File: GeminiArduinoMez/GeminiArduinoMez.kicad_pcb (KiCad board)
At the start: 2 copper layers, 99.1 x 81.3 mm, 21 parts, among them J1 Conn_01x10, J2 CONN_06SILK_FEMALE_PTH, J3 CONN_06SILK_FEMALE_PTH, J4 Conn_02x10_Odd_Even, J5 POWER, J6 Switch, M1 Left MOTOR, M2 Right MOTOR, U1 DFRobot_DC_Controller

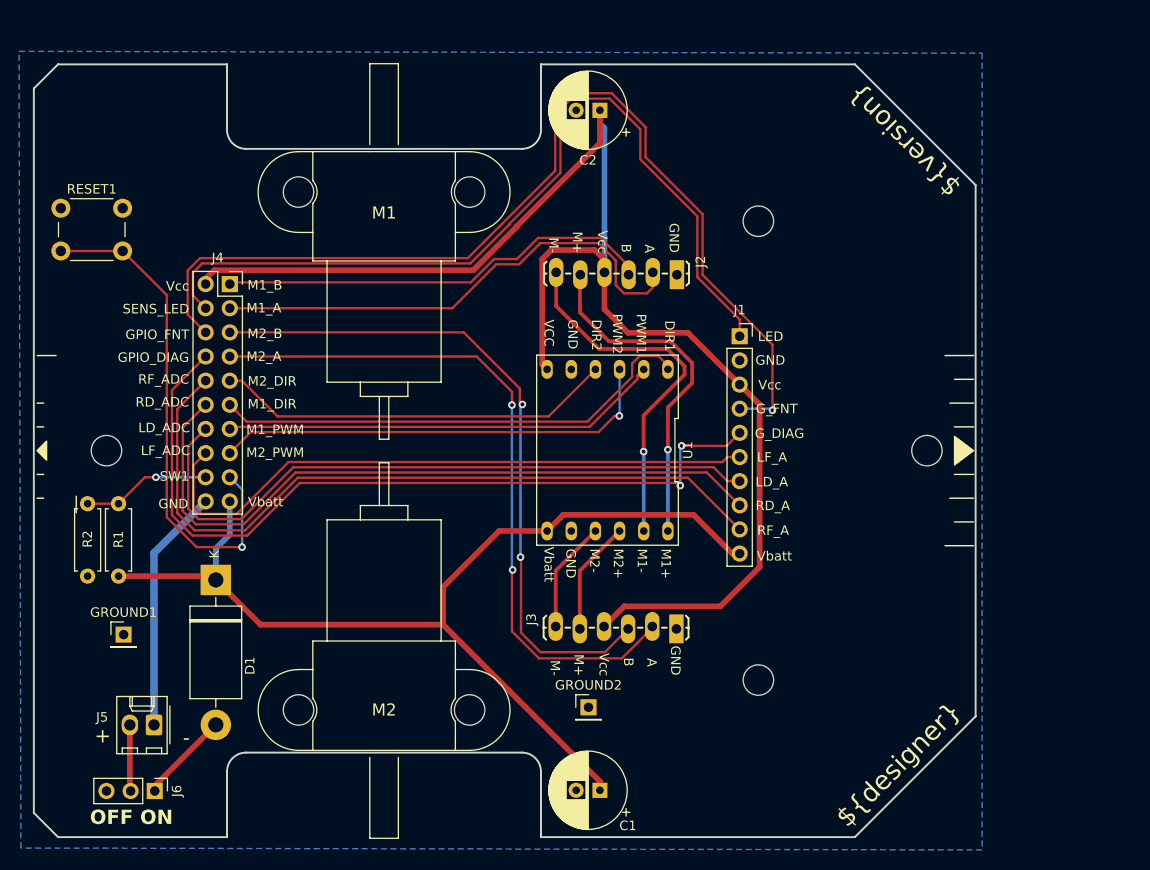
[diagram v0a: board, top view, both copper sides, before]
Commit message: Version 2 of boards sent to JLCPCB and a new calibration board
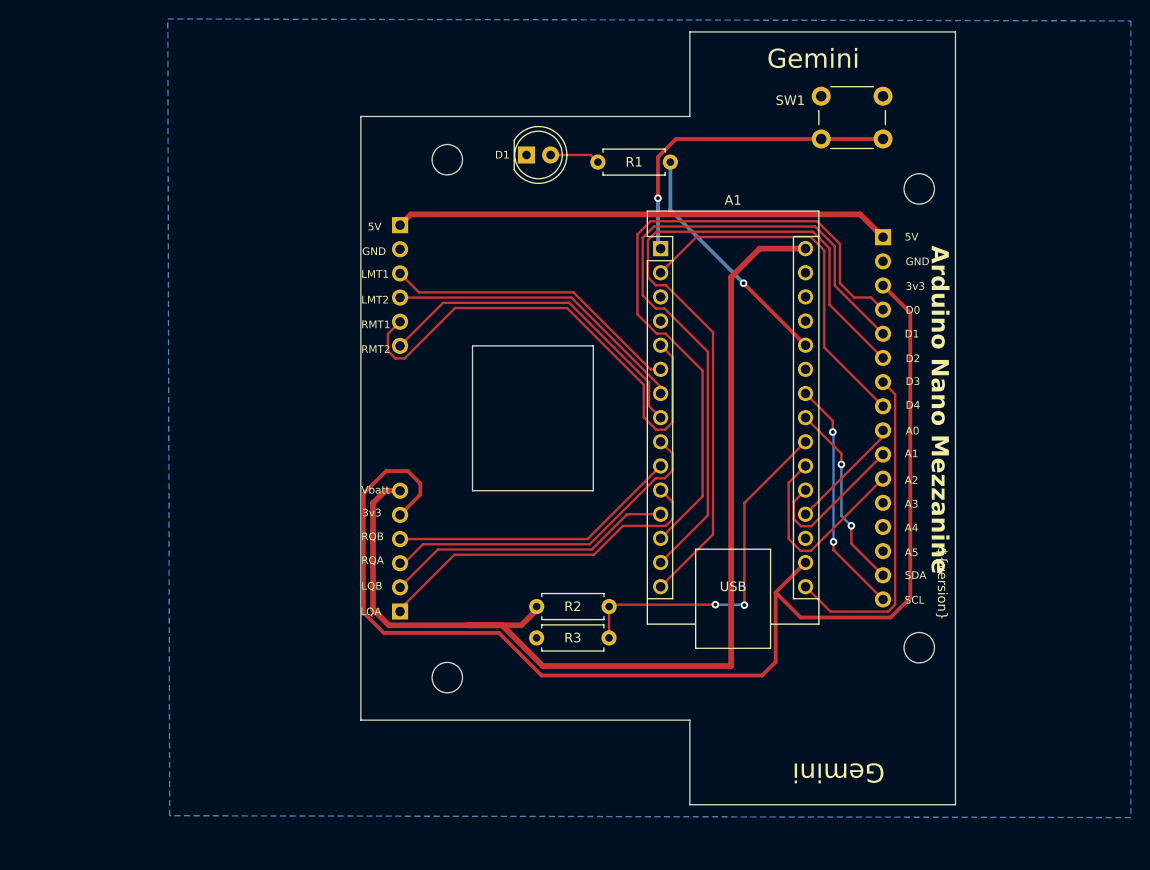
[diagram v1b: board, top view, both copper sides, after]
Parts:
- removed C1, C2: 330uF, 16V, Capacitor_THT:CP_Radial_D8.0mm_P2.50mm
- removed GROUND1, GROUND2: GROUND, Connector_PinHeader_2.54mm:PinHeader_1x01_P2.54mm_Vertical
- removed J2: CONN_06SILK_FEMALE_PTH, ukmarsbot:1X06_LOCK_LONGPADS
- removed J5: POWER, Connector_Molex:Molex_KK-254_AE-6410-02A_1x02_P2.54mm_Vertical
- removed J6: Switch, Connector_PinHeader_2.54mm:PinHeader_1x03_P2.54mm_Vertical
- removed M1: Left MOTOR, ukmarsbot:MINI-METAL-GEARMOTOR-WITH-BRACKET_Alt
- removed M2: Right MOTOR, ukmarsbot:MINI-METAL-GEARMOTOR-WITH-BRACKET
- removed RESET1: TACT_SW, Button_Switch_THT:SW_PUSH_6mm
- removed U1: DFRobot_DC_Controller, PBFootPrintLibrary:DFRobot_DC_Controller
- added A1: Arduino_Nano_RP2040_Connect, Module:Arduino_Nano, F.Cu at (134.1, 83.8)
- added R3: 68K, Resistor_THT:R_Axial_DIN0207_L6.3mm_D2.5mm_P7.62mm_Horizontal, F.Cu at (128.7, 124.7)
- added SW1: TACT_SW, Button_Switch_THT:SW_PUSH_6mm, F.Cu at (151.0, 67.7)
- D1: value 1N5401 -> LED; footprint Diode_THT:D_DO-201AD_P15.24mm_Horizontal -> LED_THT:LED_D5.0mm
- J1: value Conn_01x10 -> Conn_01x16; footprint Connector_PinSocket_2.54mm:PinSocket_1x10_P2.54mm_Vertical -> Connector_PinHeader_2.54mm:PinHeader_1x16_P2.54mm_Vertical; moved to B.Cu
- J3: value CONN_06SILK_FEMALE_PTH -> Conn_01x06; footprint ukmarsbot:1X06_LOCK_LONGPADS -> Connector_PinHeader_2.54mm:PinHeader_1x06_P2.54mm_Vertical; moved to B.Cu
- J4: value Conn_02x10_Odd_Even -> Conn_01x06; footprint Connector_PinSocket_2.54mm:PinSocket_2x10_P2.54mm_Vertical -> Connector_PinHeader_2.54mm:PinHeader_1x06_P2.54mm_Vertical; moved to B.Cu
- R1: value 180K -> 680R
- R2: value 68K -> 180K
- moved R1 72.6 mm to (135.1, 74.7), turned to 180 degrees
- moved H2 55.8 mm to (111.7, 128.9)
- moved D1 55.4 mm to (120.0, 73.9), turned to 0 degrees
- moved J3 51.5 mm to (106.7, 81.3), turned to 180 degrees
- moved R2 48.5 mm to (121.0, 121.4), turned to 0 degrees
- moved H1 47.1 mm to (111.7, 74.4)
- moved J4 38.8 mm to (106.7, 121.9)
- moved J1 18.3 mm to (157.5, 82.5), turned to 180 degrees
- moved H3 17.3 mm to (161.3, 77.5)
- moved H4 17.3 mm to (161.3, 125.7)
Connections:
- D1 pad 1: Vbatt -> GND
- D1 pad 2: /PWR -> Net-(D1-A)
- J1 pad 1: SENSOR_LED -> 5V
- J1 pad 10: Vbatt -> SEN1AIP
- J1 pad 3: Vcc -> 3v3
- J1 pad 4: GPIO_FRONT -> SEN0DI0
- J1 pad 5: GPIO_DIAG -> SEN1DI0
- J1 pad 6: LEFT_FRONT_ADC -> SEN2DI0
- J1 pad 7: LEFT_DIAG_ADC -> SEN3DI0
- J1 pad 8: RIGHT_DIAG_ADC -> SEN4DI0
- J1 pad 9: RIGHT_FRONT_ADC -> SEN0AIP
- J3 pad 1: GND -> 5V
- J3 pad 2: RIGHT_ENC_A -> GND
- J3 pad 3: RIGHT_ENC_B -> LMTR1
- J3 pad 4: Vcc -> LMTR2
- J3 pad 5: RIGHT_MOTOR_1 -> RMTR1
- J3 pad 6: RIGHT_MOTOR_2 -> RMTR2
- J4 pad 1: LEFT_ENC_B -> LQA
- J4 pad 2: Vcc -> LQB
- J4 pad 3: LEFT_ENC_A -> RQA
- J4 pad 4: SENSOR_LED -> RQB
- J4 pad 5: RIGHT_ENC_B -> 3v3
- J4 pad 6: GPIO_FRONT -> Vbatt
- R1 pad 1: Vbatt -> GPIO10
- R1 pad 2: D18_A6 -> Net-(D1-A)
- R2 pad 1: D18_A6 -> Vbatt
- R2 pad 2: GND -> SEN3AIP
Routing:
- net Vcc: track 149.7 -> 0.00 mm
- net 3v3: track 0.00 -> 132.7 mm
- net GPIO_FRONT: track 107.4 -> 0.00 mm, vias 1 -> 0
- net SENSOR_LED: track 90.3 -> 0.00 mm
- net GPIO_DIAG: track 85.8 -> 0.00 mm, vias 2 -> 0
- net RIGHT_FRONT_ADC: track 79.6 -> 0.00 mm
- net SEN2DI0: track 0.00 -> 76.3 mm
- net RIGHT_DIAG_ADC: track 75.0 -> 0.00 mm
- net RIGHT_ENC_A: track 73.9 -> 0.00 mm, vias 2 -> 0
- net SEN1DI0: track 0.00 -> 72.5 mm
- net RIGHT_ENC_B: track 72.0 -> 0.00 mm, vias 2 -> 0
- net LEFT_DIAG_ADC: track 70.5 -> 0.00 mm
- net SEN0DI0: track 0.00 -> 69.9 mm
- net LEFT_FRONT_ADC: track 66.4 -> 0.00 mm
- net RESET: track 53.5 -> 0.00 mm, vias 1 -> 0
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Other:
- board size 99.1 x 81.3 mm -> 62.5 x 81.3 mm
- board text added: "3v3"
- board text added: "5V"
- board text added: "A0"
- board text added: "A1"
- board text added: "A2"
- board text added: "A3"
- board text added: "A4"
- board text added: "A5"
- board text added: "Arduino Nano Mezzanine"
- board text added: "Bottom"
- board text added: "D0"
- board text added: "D1"
- board text added: "D2"
- board text added: "D3"
- board text added: "D4"
- board text added: "Gemini"
- board text added: "LMT1"
- board text added: "LMT2"
- board text added: "LQA"
- board text added: "LQB"
- board text added: "RMT1"
- board text added: "RMT2"
- board text added: "RQA"
- board text added: "RQB"
- board text added: "SCL"
- board text added: "SDA"
- board text removed: "${designer}"
- board text removed: "+"
- board text removed: "-"
- board text removed: "A"
- board text removed: "B"
- board text removed: "GPIO_DIAG"
- board text removed: "GPIO_FNT"
- board text removed: "G_DIAG"
- board text removed: "G_FNT"
- board text removed: "LD_A"
- board text removed: "LD_ADC"
- board text removed: "LED"
- board text removed: "LF_A"
- board text removed: "LF_ADC"
- board text removed: "M+"
- board text removed: "M-"
- board text removed: "M1_A"
- board text removed: "M1_B"
- board text removed: "M1_DIR"
- board text removed: "M1_PWM"
- board text removed: "M2_A"
- board text removed: "M2_B"
- board text removed: "M2_DIR"
- board text removed: "M2_PWM"
- board text removed: "OFF ON"
- board text removed: "Please Turn Over"
- board text removed: "RD_A"
- board text removed: "RD_ADC"
- board text removed: "RF_A"
- board text removed: "RF_ADC"
- board text removed: "SENS_LED"
- board text removed: "SERPENT SCAMPER"
- board text removed: "SW1"
- board text removed: "Vcc"
